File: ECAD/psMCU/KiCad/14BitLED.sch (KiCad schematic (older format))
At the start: 28 parts

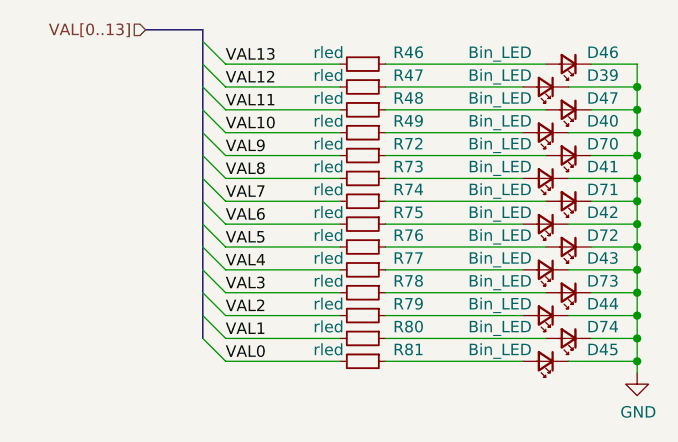
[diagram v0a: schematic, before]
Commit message: First draft v1.0 schematic done, ready for verify
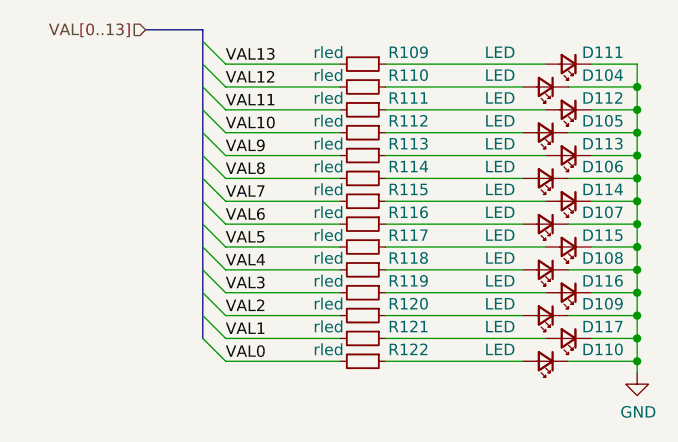
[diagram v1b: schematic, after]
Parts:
- D104, D105, D106, D107, D108, D109, D110, D111, D112, D113, D114, D115, D116, D117: value Bin_LED -> LED

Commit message: Annotation.
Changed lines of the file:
@@
 AR Path="/5FD6EE9C/608FE1FD/6094AACA/600C3881" Ref="R?"  Part="1"
 AR Path="/5FD6F3D6/618A42E6/600C3881" Ref="R73"  Part="1"
-F 0 "R114" V 4350 2350 50  0000 C CNN
+F 0 "R17" V 4350 2350 50  0000 C CNN
 F 1 "rled" V 4350 2000 50  0000 C CNN
 F 2 "NoRef_Footprints:R_0603_1608Metric_NoRef" H 4400 2150 50  0001 C CNN
@@
 AR Path="/5FD6EE9C/608FE1FD/6094AACA/600C3882" Ref="R?"  Part="1"
 AR Path="/5FD6F3D6/618A42E6/600C3882" Ref="R74"  Part="1"
-F 0 "R115" V 4350 2450 50  0000 C CNN
+F 0 "R18" V 4350 2450 50  0000 C CNN
 F 1 "rled" V 4350 2100 50  0000 C CNN
 F 2 "NoRef_Footprints:R_0603_1608Metric_NoRef" H 4400 2250 50  0001 C CNN
@@
 AR Path="/5FD6EE9C/608FE1FD/6094AACA/600C3883" Ref="R?"  Part="1"
 AR Path="/5FD6F3D6/618A42E6/600C3883" Ref="R75"  Part="1"
-F 0 "R116" V 4350 2550 50  0000 C CNN
+F 0 "R19" V 4350 2550 50  0000 C CNN
 F 1 "rled" V 4350 2200 50  0000 C CNN
 F 2 "NoRef_Footprints:R_0603_1608Metric_NoRef" H 4400 2350 50  0001 C CNN
@@
 AR Path="/5FD6EE9C/608FE1FD/6094AACA/600C3884" Ref="R?"  Part="1"
 AR Path="/5FD6F3D6/618A42E6/600C3884" Ref="R76"  Part="1"
-F 0 "R117" V 4350 2650 50  0000 C CNN
+F 0 "R20" V 4350 2650 50  0000 C CNN
 F 1 "rled" V 4350 2300 50  0000 C CNN
 F 2 "NoRef_Footprints:R_0603_1608Metric_NoRef" H 4400 2450 50  0001 C CNN
@@
 AR Path="/5FD6EE9C/608FE1FD/6094AACA/6041A801" Ref="R?"  Part="1"
 AR Path="/5FD6F3D6/618A42E6/6041A801" Ref="R77"  Part="1"
-F 0 "R118" V 4350 2750 50  0000 C CNN
+F 0 "R21" V 4350 2750 50  0000 C CNN
 F 1 "rled" V 4350 2400 50  0000 C CNN
 F 2 "NoRef_Footprints:R_0603_1608Metric_NoRef" H 4400 2550 50  0001 C CNN
@@
 AR Path="/5FD6EE9C/608FE1FD/6094AACA/6048F34A" Ref="R?"  Part="1"
 AR Path="/5FD6F3D6/618A42E6/6048F34A" Ref="R78"  Part="1"
-F 0 "R119" V 4350 2850 50  0000 C CNN
+F 0 "R22" V 4350 2850 50  0000 C CNN
 F 1 "rled" V 4350 2500 50  0000 C CNN
 F 2 "NoRef_Footprints:R_0603_1608Metric_NoRef" H 4400 2650 50  0001 C CNN
@@
 AR Path="/5FD6EE9C/608FE1FD/6094AACA/600C3886" Ref="R?"  Part="1"
 AR Path="/5FD6F3D6/618A42E6/600C3886" Ref="R79"  Part="1"
-F 0 "R120" V 4350 2950 50  0000 C CNN
+F 0 "R23" V 4350 2950 50  0000 C CNN
 F 1 "rled" V 4350 2600 50  0000 C CNN
 F 2 "NoRef_Footprints:R_0603_1608Metric_NoRef" H 4400 2750 50  0001 C CNN
@@
 AR Path="/5FD6EE9C/608FE1FD/6094AACA/600C3887" Ref="R?"  Part="1"
 AR Path="/5FD6F3D6/618A42E6/600C3887" Ref="R80"  Part="1"
-F 0 "R121" V 4350 3050 50  0000 C CNN
+F 0 "R24" V 4350 3050 50  0000 C CNN
 F 1 "rled" V 4350 2700 50  0000 C CNN
 F 2 "NoRef_Footprints:R_0603_1608Metric_NoRef" H 4400 2850 50  0001 C CNN
@@
 AR Path="/5FD6EE9C/608FE1FD/6094AACA/600C388C" Ref="D?"  Part="1"
 AR Path="/5FD6F3D6/618A42E6/600C388C" Ref="D41"  Part="1"
-F 0 "D106" H 4950 2100 50  0000 C CNN
+F 0 "D13" H 4950 2100 50  0000 C CNN
 F 1 "LED" H 5400 2100 50  0000 C CNN
 F 2 "NoRef_Footprints:D_0603_1608Metric_NoRef" V 5200 2150 50  0001 C CNN
@@
 AR Path="/5FD6EE9C/608FE1FD/6094AACA/600C388D" Ref="D?"  Part="1"
 AR Path="/5FD6F3D6/618A42E6/600C388D" Ref="D71"  Part="1"
-F 0 "D114" H 5150 2200 50  0000 C CNN
+F 0 "D21" H 5150 2200 50  0000 C CNN
 F 1 "LED" H 5600 2200 50  0000 C CNN
 F 2 "NoRef_Footprints:D_0603_1608Metric_NoRef" V 5300 2250 50  0001 C CNN
@@
 AR Path="/5FD6EE9C/608FE1FD/6094AACA/600C387D" Ref="D?"  Part="1"
 AR Path="/5FD6F3D6/618A42E6/600C387D" Ref="D42"  Part="1"
-F 0 "D107" H 4950 2300 50  0000 C CNN
+F 0 "D14" H 4950 2300 50  0000 C CNN
 F 1 "LED" H 5400 2300 50  0000 C CNN
 F 2 "NoRef_Footprints:D_0603_1608Metric_NoRef" V 5200 2350 50  0001 C CNN
@@
 AR Path="/5FD6EE9C/608FE1FD/6094AACA/600C3889" Ref="D?"  Part="1"
 AR Path="/5FD6F3D6/618A42E6/600C3889" Ref="D72"  Part="1"
-F 0 "D115" H 5150 2400 50  0000 C CNN
+F 0 "D22" H 5150 2400 50  0000 C CNN
 F 1 "LED" H 5600 2400 50  0000 C CNN
 F 2 "NoRef_Footprints:D_0603_1608Metric_NoRef" V 5300 2450 50  0001 C CNN
@@
 AR Path="/5FD6EE9C/608FE1FD/6094AACA/600C388A" Ref="D?"  Part="1"
 AR Path="/5FD6F3D6/618A42E6/600C388A" Ref="D43"  Part="1"
-F 0 "D108" H 4950 2500 50  0000 C CNN
+F 0 "D15" H 4950 2500 50  0000 C CNN
 F 1 "LED" H 5400 2500 50  0000 C CNN
 F 2 "NoRef_Footprints:D_0603_1608Metric_NoRef" V 5200 2550 50  0001 C CNN
@@
 AR Path="/5FD6EE9C/608FE1FD/6094AACA/6041A7F8" Ref="D?"  Part="1"
 AR Path="/5FD6F3D6/618A42E6/6041A7F8" Ref="D73"  Part="1"
-F 0 "D116" H 5150 2600 50  0000 C CNN
+F 0 "D23" H 5150 2600 50  0000 C CNN
 F 1 "LED" H 5600 2600 50  0000 C CNN
 F 2 "NoRef_Footprints:D_0603_1608Metric_NoRef" V 5300 2650 50  0001 C CNN
@@
 AR Path="/5FD6EE9C/608FE1FD/6094AACA/5F5C70EC" Ref="D?"  Part="1"
 AR Path="/5FD6F3D6/618A42E6/5F5C70EC" Ref="D44"  Part="1"
-F 0 "D109" H 4950 2700 50  0000 C CNN
+F 0 "D16" H 4950 2700 50  0000 C CNN
 F 1 "LED" H 5400 2700 50  0000 C CNN
 F 2 "NoRef_Footprints:D_0603_1608Metric_NoRef" V 5200 2750 50  0001 C CNN
@@
 AR Path="/5FD6EE9C/608FE1FD/6094AACA/6041A7FA" Ref="D?"  Part="1"
 AR Path="/5FD6F3D6/618A42E6/6041A7FA" Ref="D74"  Part="1"
-F 0 "D117" H 5150 2800 50  0000 C CNN
+F 0 "D24" H 5150 2800 50  0000 C CNN
 F 1 "LED" H 5600 2800 50  0000 C CNN
 F 2 "NoRef_Footprints:D_0603_1608Metric_NoRef" V 5300 2850 50  0001 C CNN
@@
 AR Path="/5FD6EE9C/608FE1FD/6094AACA/600C3888" Ref="#PWR?"  Part="1"
 AR Path="/5FD6F3D6/618A42E6/600C3888" Ref="#PWR0358"  Part="1"
-F 0 "#PWR0481" H 5600 2750 50  0001 C CNN
+F 0 "#PWR0175" H 5600 2750 50  0001 C CNN
 F 1 "GND" H 5605 2827 50  0000 C CNN
 F 2 "" H 5600 3000 50  0001 C CNN
@@
 AR Path="/5FD6EE9C/608FE1FD/6094AACA/600C3880" Ref="R?"  Part="1"
 AR Path="/5FD6F3D6/618A42E6/600C3880" Ref="R81"  Part="1"
-F 0 "R122" V 4350 3150 50  0000 C CNN
+F 0 "R25" V 4350 3150 50  0000 C CNN
 F 1 "rled" V 4350 2800 50  0000 C CNN
 F 2 "NoRef_Footprints:R_0603_1608Metric_NoRef" H 4400 2950 50  0001 C CNN
@@
 AR Path="/5FD6EE9C/608FE1FD/6094AACA/6036725D" Ref="D?"  Part="1"
 AR Path="/5FD6F3D6/618A42E6/6036725D" Ref="D45"  Part="1"
-F 0 "D110" H 4950 2900 50  0000 C CNN
+F 0 "D17" H 4950 2900 50  0000 C CNN
 F 1 "LED" H 5400 2900 50  0000 C CNN
 F 2 "NoRef_Footprints:D_0603_1608Metric_NoRef" V 5200 2950 50  0001 C CNN
@@
 AR Path="/5FD6EE9C/608FE1FD/6094AACA/600C3873" Ref="R?"  Part="1"
 AR Path="/5FD6F3D6/618A42E6/600C3873" Ref="R49"  Part="1"
-F 0 "R112" V 4350 2150 50  0000 C CNN
+F 0 "R15" V 4350 2150 50  0000 C CNN
 F 1 "rled" V 4350 1800 50  0000 C CNN
 F 2 "NoRef_Footprints:R_0603_1608Metric_NoRef" H 4400 1950 50  0001 C CNN
@@
 AR Path="/5FD6EE9C/608FE1FD/6094AACA/6038A9CB" Ref="R?"  Part="1"
 AR Path="/5FD6F3D6/618A42E6/6038A9CB" Ref="R72"  Part="1"
-F 0 "R113" V 4350 2250 50  0000 C CNN
+F 0 "R16" V 4350 2250 50  0000 C CNN
 F 1 "rled" V 4350 1900 50  0000 C CNN
 F 2 "NoRef_Footprints:R_0603_1608Metric_NoRef" H 4400 2050 50  0001 C CNN
@@
 AR Path="/5FD6EE9C/608FE1FD/6094AACA/6038A9D2" Ref="D?"  Part="1"
 AR Path="/5FD6F3D6/618A42E6/6038A9D2" Ref="D40"  Part="1"
-F 0 "D105" H 4950 1900 50  0000 C CNN
+F 0 "D12" H 4950 1900 50  0000 C CNN
 F 1 "LED" H 5400 1900 50  0000 C CNN
 F 2 "NoRef_Footprints:D_0603_1608Metric_NoRef" V 5200 1950 50  0001 C CNN
@@
 AR Path="/5FD6EE9C/608FE1FD/6094AACA/6038A9D8" Ref="D?"  Part="1"
 AR Path="/5FD6F3D6/618A42E6/6038A9D8" Ref="D70"  Part="1"
-F 0 "D113" H 5150 2000 50  0000 C CNN
+F 0 "D20" H 5150 2000 50  0000 C CNN
 F 1 "LED" H 5600 2000 50  0000 C CNN
 F 2 "NoRef_Footprints:D_0603_1608Metric_NoRef" V 5300 2050 50  0001 C CNN
@@
 AR Path="/5FD6EE9C/608FE1FD/6094AACA/600C3877" Ref="R?"  Part="1"
 AR Path="/5FD6F3D6/618A42E6/600C3877" Ref="R47"  Part="1"
-F 0 "R110" V 4350 1950 50  0000 C CNN
+F 0 "R13" V 4350 1950 50  0000 C CNN
 F 1 "rled" V 4350 1600 50  0000 C CNN
 F 2 "NoRef_Footprints:R_0603_1608Metric_NoRef" H 4400 1750 50  0001 C CNN
@@
 AR Path="/5FD6EE9C/608FE1FD/6094AACA/600C3878" Ref="R?"  Part="1"
 AR Path="/5FD6F3D6/618A42E6/600C3878" Ref="R48"  Part="1"
-F 0 "R111" V 4350 2050 50  0000 C CNN
+F 0 "R14" V 4350 2050 50  0000 C CNN
 F 1 "rled" V 4350 1700 50  0000 C CNN
 F 2 "NoRef_Footprints:R_0603_1608Metric_NoRef" H 4400 1850 50  0001 C CNN
@@
 AR Path="/5FD6EE9C/608FE1FD/6094AACA/6038C68F" Ref="D?"  Part="1"
 AR Path="/5FD6F3D6/618A42E6/6038C68F" Ref="D39"  Part="1"
-F 0 "D104" H 4950 1700 50  0000 C CNN
+F 0 "D11" H 4950 1700 50  0000 C CNN
 F 1 "LED" H 5400 1700 50  0000 C CNN
 F 2 "NoRef_Footprints:D_0603_1608Metric_NoRef" V 5200 1750 50  0001 C CNN
@@
 AR Path="/5FD6EE9C/608FE1FD/6094AACA/6038C695" Ref="D?"  Part="1"
 AR Path="/5FD6F3D6/618A42E6/6038C695" Ref="D47"  Part="1"
-F 0 "D112" H 5150 1800 50  0000 C CNN
+F 0 "D19" H 5150 1800 50  0000 C CNN
 F 1 "LED" H 5600 1800 50  0000 C CNN
 F 2 "NoRef_Footprints:D_0603_1608Metric_NoRef" V 5300 1850 50  0001 C CNN
@@
 AR Path="/5FD6EE9C/608FE1FD/6094AACA/600C387B" Ref="R?"  Part="1"
 AR Path="/5FD6F3D6/618A42E6/600C387B" Ref="R46"  Part="1"
-F 0 "R109" V 4350 1850 50  0000 C CNN
+F 0 "R12" V 4350 1850 50  0000 C CNN
 F 1 "rled" V 4350 1500 50  0000 C CNN
 F 2 "NoRef_Footprints:R_0603_1608Metric_NoRef" H 4400 1650 50  0001 C CNN
@@
 AR Path="/5FD6EE9C/608FE1FD/6094AACA/600C387C" Ref="D?"  Part="1"
 AR Path="/5FD6F3D6/618A42E6/600C387C" Ref="D46"  Part="1"
-F 0 "D111" H 5150 1600 50  0000 C CNN
+F 0 "D18" H 5150 1600 50  0000 C CNN
 F 1 "LED" H 5600 1600 50  0000 C CNN
 F 2 "NoRef_Footprints:D_0603_1608Metric_NoRef" V 5300 1650 50  0001 C CNN

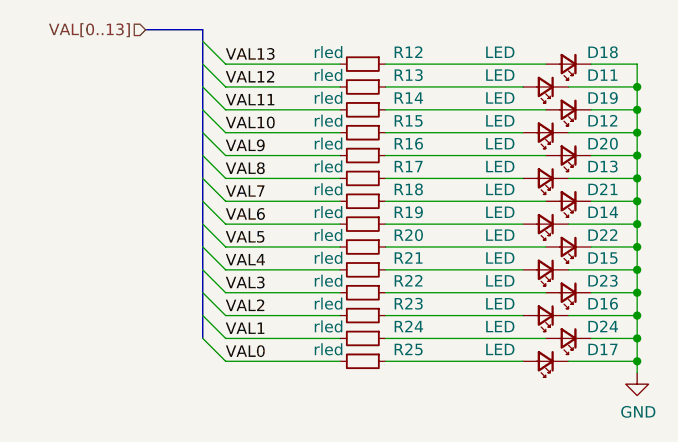
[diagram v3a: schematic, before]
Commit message: Simplified Barrel Shifter
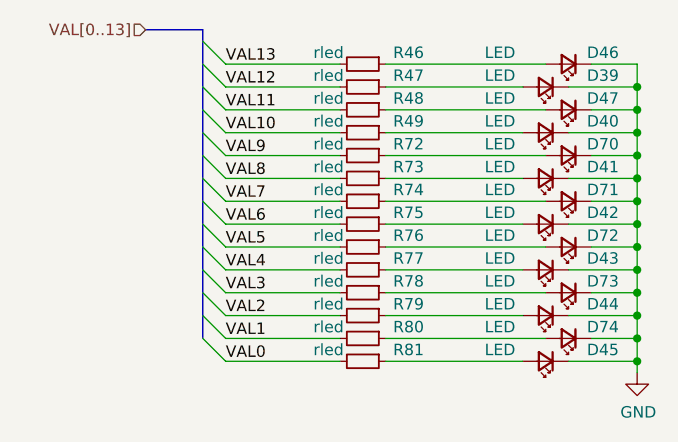
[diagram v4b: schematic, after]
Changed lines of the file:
@@
 AR Path="/5FD6EE9C/608FE1FD/6094AACA/600C3881" Ref="R?"  Part="1"
 AR Path="/5FD6F3D6/618A42E6/600C3881" Ref="R73"  Part="1"
-F 0 "R17" V 4350 2350 50  0000 C CNN
+F 0 "R73" V 4350 2350 50  0000 C CNN
 F 1 "rled" V 4350 2000 50  0000 C CNN
 F 2 "NoRef_Footprints:R_0603_1608Metric_NoRef" H 4400 2150 50  0001 C CNN
@@
 AR Path="/5FD6EE9C/608FE1FD/6094AACA/600C3882" Ref="R?"  Part="1"
 AR Path="/5FD6F3D6/618A42E6/600C3882" Ref="R74"  Part="1"
-F 0 "R18" V 4350 2450 50  0000 C CNN
+F 0 "R74" V 4350 2450 50  0000 C CNN
 F 1 "rled" V 4350 2100 50  0000 C CNN
 F 2 "NoRef_Footprints:R_0603_1608Metric_NoRef" H 4400 2250 50  0001 C CNN
@@
 AR Path="/5FD6EE9C/608FE1FD/6094AACA/600C3883" Ref="R?"  Part="1"
 AR Path="/5FD6F3D6/618A42E6/600C3883" Ref="R75"  Part="1"
-F 0 "R19" V 4350 2550 50  0000 C CNN
+F 0 "R75" V 4350 2550 50  0000 C CNN
 F 1 "rled" V 4350 2200 50  0000 C CNN
 F 2 "NoRef_Footprints:R_0603_1608Metric_NoRef" H 4400 2350 50  0001 C CNN
@@
 AR Path="/5FD6EE9C/608FE1FD/6094AACA/600C3884" Ref="R?"  Part="1"
 AR Path="/5FD6F3D6/618A42E6/600C3884" Ref="R76"  Part="1"
-F 0 "R20" V 4350 2650 50  0000 C CNN
+F 0 "R76" V 4350 2650 50  0000 C CNN
 F 1 "rled" V 4350 2300 50  0000 C CNN
 F 2 "NoRef_Footprints:R_0603_1608Metric_NoRef" H 4400 2450 50  0001 C CNN
@@
 AR Path="/5FD6EE9C/608FE1FD/6094AACA/6041A801" Ref="R?"  Part="1"
 AR Path="/5FD6F3D6/618A42E6/6041A801" Ref="R77"  Part="1"
-F 0 "R21" V 4350 2750 50  0000 C CNN
+F 0 "R77" V 4350 2750 50  0000 C CNN
 F 1 "rled" V 4350 2400 50  0000 C CNN
 F 2 "NoRef_Footprints:R_0603_1608Metric_NoRef" H 4400 2550 50  0001 C CNN
@@
 AR Path="/5FD6EE9C/608FE1FD/6094AACA/6048F34A" Ref="R?"  Part="1"
 AR Path="/5FD6F3D6/618A42E6/6048F34A" Ref="R78"  Part="1"
-F 0 "R22" V 4350 2850 50  0000 C CNN
+F 0 "R78" V 4350 2850 50  0000 C CNN
 F 1 "rled" V 4350 2500 50  0000 C CNN
 F 2 "NoRef_Footprints:R_0603_1608Metric_NoRef" H 4400 2650 50  0001 C CNN
@@
 AR Path="/5FD6EE9C/608FE1FD/6094AACA/600C3886" Ref="R?"  Part="1"
 AR Path="/5FD6F3D6/618A42E6/600C3886" Ref="R79"  Part="1"
-F 0 "R23" V 4350 2950 50  0000 C CNN
+F 0 "R79" V 4350 2950 50  0000 C CNN
 F 1 "rled" V 4350 2600 50  0000 C CNN
 F 2 "NoRef_Footprints:R_0603_1608Metric_NoRef" H 4400 2750 50  0001 C CNN
@@
 AR Path="/5FD6EE9C/608FE1FD/6094AACA/600C3887" Ref="R?"  Part="1"
 AR Path="/5FD6F3D6/618A42E6/600C3887" Ref="R80"  Part="1"
-F 0 "R24" V 4350 3050 50  0000 C CNN
+F 0 "R80" V 4350 3050 50  0000 C CNN
 F 1 "rled" V 4350 2700 50  0000 C CNN
 F 2 "NoRef_Footprints:R_0603_1608Metric_NoRef" H 4400 2850 50  0001 C CNN
@@
 AR Path="/5FD6EE9C/608FE1FD/6094AACA/600C388C" Ref="D?"  Part="1"
 AR Path="/5FD6F3D6/618A42E6/600C388C" Ref="D41"  Part="1"
-F 0 "D13" H 4950 2100 50  0000 C CNN
+F 0 "D41" H 4950 2100 50  0000 C CNN
 F 1 "LED" H 5400 2100 50  0000 C CNN
 F 2 "NoRef_Footprints:D_0603_1608Metric_NoRef" V 5200 2150 50  0001 C CNN
@@
 AR Path="/5FD6EE9C/608FE1FD/6094AACA/600C388D" Ref="D?"  Part="1"
 AR Path="/5FD6F3D6/618A42E6/600C388D" Ref="D71"  Part="1"
-F 0 "D21" H 5150 2200 50  0000 C CNN
+F 0 "D71" H 5150 2200 50  0000 C CNN
 F 1 "LED" H 5600 2200 50  0000 C CNN
 F 2 "NoRef_Footprints:D_0603_1608Metric_NoRef" V 5300 2250 50  0001 C CNN
@@
 AR Path="/5FD6EE9C/608FE1FD/6094AACA/600C387D" Ref="D?"  Part="1"
 AR Path="/5FD6F3D6/618A42E6/600C387D" Ref="D42"  Part="1"
-F 0 "D14" H 4950 2300 50  0000 C CNN
+F 0 "D42" H 4950 2300 50  0000 C CNN
 F 1 "LED" H 5400 2300 50  0000 C CNN
 F 2 "NoRef_Footprints:D_0603_1608Metric_NoRef" V 5200 2350 50  0001 C CNN
@@
 AR Path="/5FD6EE9C/608FE1FD/6094AACA/600C3889" Ref="D?"  Part="1"
 AR Path="/5FD6F3D6/618A42E6/600C3889" Ref="D72"  Part="1"
-F 0 "D22" H 5150 2400 50  0000 C CNN
+F 0 "D72" H 5150 2400 50  0000 C CNN
 F 1 "LED" H 5600 2400 50  0000 C CNN
 F 2 "NoRef_Footprints:D_0603_1608Metric_NoRef" V 5300 2450 50  0001 C CNN
@@
 AR Path="/5FD6EE9C/608FE1FD/6094AACA/600C388A" Ref="D?"  Part="1"
 AR Path="/5FD6F3D6/618A42E6/600C388A" Ref="D43"  Part="1"
-F 0 "D15" H 4950 2500 50  0000 C CNN
+F 0 "D43" H 4950 2500 50  0000 C CNN
 F 1 "LED" H 5400 2500 50  0000 C CNN
 F 2 "NoRef_Footprints:D_0603_1608Metric_NoRef" V 5200 2550 50  0001 C CNN
@@
 AR Path="/5FD6EE9C/608FE1FD/6094AACA/6041A7F8" Ref="D?"  Part="1"
 AR Path="/5FD6F3D6/618A42E6/6041A7F8" Ref="D73"  Part="1"
-F 0 "D23" H 5150 2600 50  0000 C CNN
+F 0 "D73" H 5150 2600 50  0000 C CNN
 F 1 "LED" H 5600 2600 50  0000 C CNN
 F 2 "NoRef_Footprints:D_0603_1608Metric_NoRef" V 5300 2650 50  0001 C CNN
@@
 AR Path="/5FD6EE9C/608FE1FD/6094AACA/5F5C70EC" Ref="D?"  Part="1"
 AR Path="/5FD6F3D6/618A42E6/5F5C70EC" Ref="D44"  Part="1"
-F 0 "D16" H 4950 2700 50  0000 C CNN
+F 0 "D44" H 4950 2700 50  0000 C CNN
 F 1 "LED" H 5400 2700 50  0000 C CNN
 F 2 "NoRef_Footprints:D_0603_1608Metric_NoRef" V 5200 2750 50  0001 C CNN
@@
 AR Path="/5FD6EE9C/608FE1FD/6094AACA/6041A7FA" Ref="D?"  Part="1"
 AR Path="/5FD6F3D6/618A42E6/6041A7FA" Ref="D74"  Part="1"
-F 0 "D24" H 5150 2800 50  0000 C CNN
+F 0 "D74" H 5150 2800 50  0000 C CNN
 F 1 "LED" H 5600 2800 50  0000 C CNN
 F 2 "NoRef_Footprints:D_0603_1608Metric_NoRef" V 5300 2850 50  0001 C CNN
@@
 AR Path="/5FD6EE9C/608FE1FD/6094AACA/600C3880" Ref="R?"  Part="1"
 AR Path="/5FD6F3D6/618A42E6/600C3880" Ref="R81"  Part="1"
-F 0 "R25" V 4350 3150 50  0000 C CNN
+F 0 "R81" V 4350 3150 50  0000 C CNN
 F 1 "rled" V 4350 2800 50  0000 C CNN
 F 2 "NoRef_Footprints:R_0603_1608Metric_NoRef" H 4400 2950 50  0001 C CNN
@@
 AR Path="/5FD6EE9C/608FE1FD/6094AACA/6036725D" Ref="D?"  Part="1"
 AR Path="/5FD6F3D6/618A42E6/6036725D" Ref="D45"  Part="1"
-F 0 "D17" H 4950 2900 50  0000 C CNN
+F 0 "D45" H 4950 2900 50  0000 C CNN
 F 1 "LED" H 5400 2900 50  0000 C CNN
 F 2 "NoRef_Footprints:D_0603_1608Metric_NoRef" V 5200 2950 50  0001 C CNN
@@
 AR Path="/5FD6EE9C/608FE1FD/6094AACA/600C3873" Ref="R?"  Part="1"
 AR Path="/5FD6F3D6/618A42E6/600C3873" Ref="R49"  Part="1"
-F 0 "R15" V 4350 2150 50  0000 C CNN
+F 0 "R49" V 4350 2150 50  0000 C CNN
 F 1 "rled" V 4350 1800 50  0000 C CNN
 F 2 "NoRef_Footprints:R_0603_1608Metric_NoRef" H 4400 1950 50  0001 C CNN
@@
 AR Path="/5FD6EE9C/608FE1FD/6094AACA/6038A9CB" Ref="R?"  Part="1"
 AR Path="/5FD6F3D6/618A42E6/6038A9CB" Ref="R72"  Part="1"
-F 0 "R16" V 4350 2250 50  0000 C CNN
+F 0 "R72" V 4350 2250 50  0000 C CNN
 F 1 "rled" V 4350 1900 50  0000 C CNN
 F 2 "NoRef_Footprints:R_0603_1608Metric_NoRef" H 4400 2050 50  0001 C CNN
@@
 AR Path="/5FD6EE9C/608FE1FD/6094AACA/6038A9D2" Ref="D?"  Part="1"
 AR Path="/5FD6F3D6/618A42E6/6038A9D2" Ref="D40"  Part="1"
-F 0 "D12" H 4950 1900 50  0000 C CNN
+F 0 "D40" H 4950 1900 50  0000 C CNN
 F 1 "LED" H 5400 1900 50  0000 C CNN
 F 2 "NoRef_Footprints:D_0603_1608Metric_NoRef" V 5200 1950 50  0001 C CNN
@@
 AR Path="/5FD6EE9C/608FE1FD/6094AACA/6038A9D8" Ref="D?"  Part="1"
 AR Path="/5FD6F3D6/618A42E6/6038A9D8" Ref="D70"  Part="1"
-F 0 "D20" H 5150 2000 50  0000 C CNN
+F 0 "D70" H 5150 2000 50  0000 C CNN
 F 1 "LED" H 5600 2000 50  0000 C CNN
 F 2 "NoRef_Footprints:D_0603_1608Metric_NoRef" V 5300 2050 50  0001 C CNN
@@
 AR Path="/5FD6EE9C/608FE1FD/6094AACA/600C3877" Ref="R?"  Part="1"
 AR Path="/5FD6F3D6/618A42E6/600C3877" Ref="R47"  Part="1"
-F 0 "R13" V 4350 1950 50  0000 C CNN
+F 0 "R47" V 4350 1950 50  0000 C CNN
 F 1 "rled" V 4350 1600 50  0000 C CNN
 F 2 "NoRef_Footprints:R_0603_1608Metric_NoRef" H 4400 1750 50  0001 C CNN
@@
 AR Path="/5FD6EE9C/608FE1FD/6094AACA/600C3878" Ref="R?"  Part="1"
 AR Path="/5FD6F3D6/618A42E6/600C3878" Ref="R48"  Part="1"
-F 0 "R14" V 4350 2050 50  0000 C CNN
+F 0 "R48" V 4350 2050 50  0000 C CNN
 F 1 "rled" V 4350 1700 50  0000 C CNN
 F 2 "NoRef_Footprints:R_0603_1608Metric_NoRef" H 4400 1850 50  0001 C CNN
@@
 AR Path="/5FD6EE9C/608FE1FD/6094AACA/6038C68F" Ref="D?"  Part="1"
 AR Path="/5FD6F3D6/618A42E6/6038C68F" Ref="D39"  Part="1"
-F 0 "D11" H 4950 1700 50  0000 C CNN
+F 0 "D39" H 4950 1700 50  0000 C CNN
 F 1 "LED" H 5400 1700 50  0000 C CNN
 F 2 "NoRef_Footprints:D_0603_1608Metric_NoRef" V 5200 1750 50  0001 C CNN
@@
 AR Path="/5FD6EE9C/608FE1FD/6094AACA/6038C695" Ref="D?"  Part="1"
 AR Path="/5FD6F3D6/618A42E6/6038C695" Ref="D47"  Part="1"
-F 0 "D19" H 5150 1800 50  0000 C CNN
+F 0 "D47" H 5150 1800 50  0000 C CNN
 F 1 "LED" H 5600 1800 50  0000 C CNN
 F 2 "NoRef_Footprints:D_0603_1608Metric_NoRef" V 5300 1850 50  0001 C CNN
@@
 AR Path="/5FD6EE9C/608FE1FD/6094AACA/600C387B" Ref="R?"  Part="1"
 AR Path="/5FD6F3D6/618A42E6/600C387B" Ref="R46"  Part="1"
-F 0 "R12" V 4350 1850 50  0000 C CNN
+F 0 "R46" V 4350 1850 50  0000 C CNN
 F 1 "rled" V 4350 1500 50  0000 C CNN
 F 2 "NoRef_Footprints:R_0603_1608Metric_NoRef" H 4400 1650 50  0001 C CNN
@@
 AR Path="/5FD6EE9C/608FE1FD/6094AACA/600C387C" Ref="D?"  Part="1"
 AR Path="/5FD6F3D6/618A42E6/600C387C" Ref="D46"  Part="1"
-F 0 "D18" H 5150 1600 50  0000 C CNN
+F 0 "D46" H 5150 1600 50  0000 C CNN
 F 1 "LED" H 5600 1600 50  0000 C CNN
 F 2 "NoRef_Footprints:D_0603_1608Metric_NoRef" V 5300 1650 50  0001 C CNN
